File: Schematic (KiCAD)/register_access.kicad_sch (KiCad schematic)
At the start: 154 parts, among them J4 NAND_7, J5 NAND_7, J6 NOR_2, J7 INVERT, J8 NOR_2, K10 NAND_2, K11 NAND_4, K12 NOR_2, K13 NAND_2, K14 NAND_4, K15 NOR_2, K16 NAND_2, K17 NAND_4, K19 NAND_4, K20 NAND_4, K21 NAND_4, K22 NAND_4, K26 NAND_4, K28 NAND_4, K29 NAND_4, K31 NAND_4, K32 NAND_4, K33 NAND_4, K35 NAND_4, K38 NAND_4, K40 NAND_4, K41 NAND_4, K42 NAND_4, K43 NAND_4, K45 NAND_4, K46 NAND_4, K49 NAND_4, K50 NAND_4, K52 NAND_4, K54 NAND_4, K56 NAND_4, K58 NAND_4, K60 NAND_4, K64 NAND_4, K65 NAND_4, K66 NAND_4, K67 NAND_4, K69 NAND_4, K71 NAND_4, K72 NOR_2, K73 NAND_2, K75 NAND_4, K76 NOR_2, K77 NAND_2, K78 NAND_4, K79 NOR_2, K8 NAND_4, K80 NAND_2, K81 NAND_4, K83 NAND_4, K85 NAND_4, K86 NAND_4, K87 NAND_4, K9 NOR_2, K91 NAND_4, K92 NAND_4, K93 NAND_4, K94 NAND_4, K95 NAND_2, K97 NAND_4

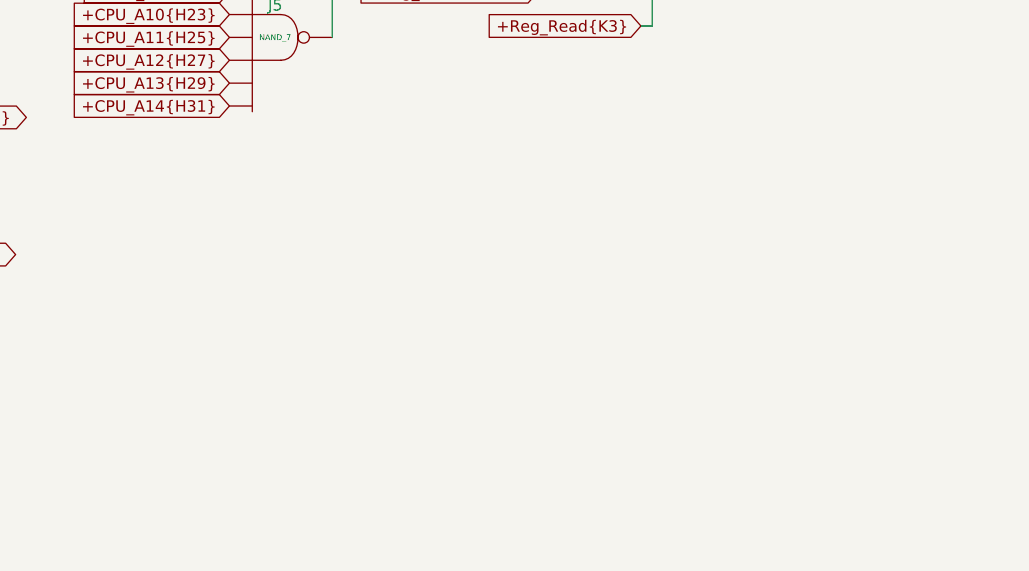
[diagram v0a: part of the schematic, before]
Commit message: - All cells in the left and center areas have now been added into the schematics.  - Changed naming of the PDF files; I was accidentally writing over furrtek's original with my new PDF.
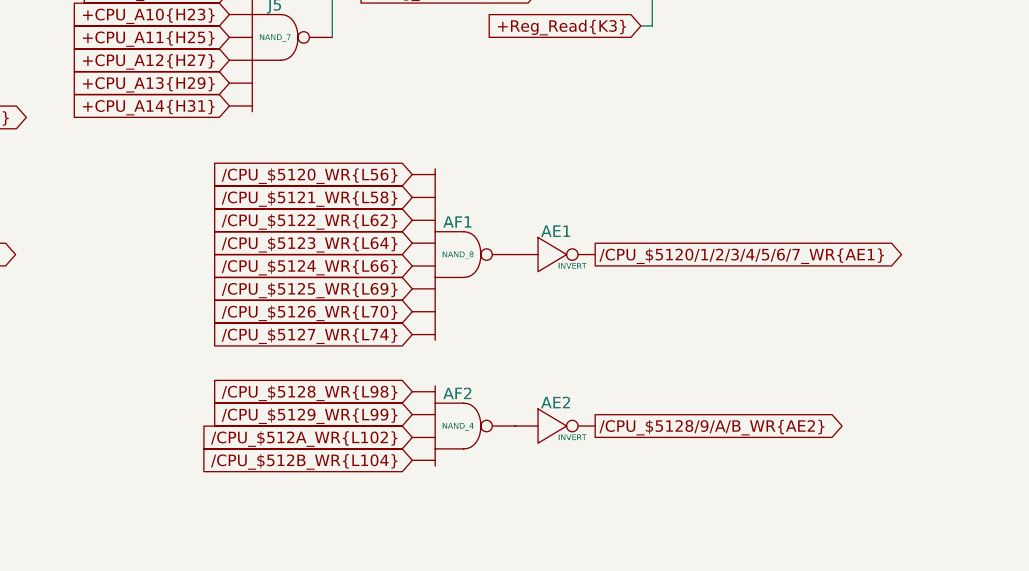
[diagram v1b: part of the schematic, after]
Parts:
- added AE1, AE2: INVERT, symbol MMC5:INVERT
- added AF1: NAND_8, symbol MMC5:NAND_8
- added AF2: NAND_4, symbol MMC5:NAND_4
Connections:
- net /CPU_$5120_WR{L56}: now also AF1. (X)
- net /CPU_$5121_WR{L58}: now also AF1. (X)
- net /CPU_$5122_WR{L62}: now also AF1. (X)
- net /CPU_$5123_WR{L64}: now also AF1. (X)
- net /CPU_$5124_WR{L66}: now also AF1. (X)
- net /CPU_$5125_WR{L69}: now also AF1. (X)
- net /CPU_$5126_WR{L70}: now also AF1. (X)
- net /CPU_$5127_WR{L74}: now also AF1. (X)
- net /CPU_$5128_WR{L98}: now also AF2. (X)
- net /CPU_$5129_WR{L99}: now also AF2. (X)
- net /CPU_$512A_WR{L102}: now also AF2. (X)
- net /CPU_$512B_WR{L104}: now also AF2. (X)
- net at J6. (X): now also J5. (X); no longer J4. (X)
- net at J7. (X): now also J8. (X); no longer J6. (X)
- new net: J4. (X), J6. (X)
- new net: J6. (X), J7. (X)
- new net: AE2. (X), AF2. (X)
- new net: K95. (X), L117. (X)
- new net: AE1. (X), AF1. (X)
- new net /CPU_$5120/1/2/3/4/5/6/7_WR{AE1}: AE1. (X)
- new net /CPU_$5128/9/A/B_WR{AE2}: AE2. (X)
